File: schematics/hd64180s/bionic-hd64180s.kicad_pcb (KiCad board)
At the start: 2 copper layers, 25.4 x 68.6 mm, 13 parts, among them J1 Bionic-P135, J2 Bionic-P245, U1 HD64180SH, U2 11AA010-I/TT, U3 74AHCT157

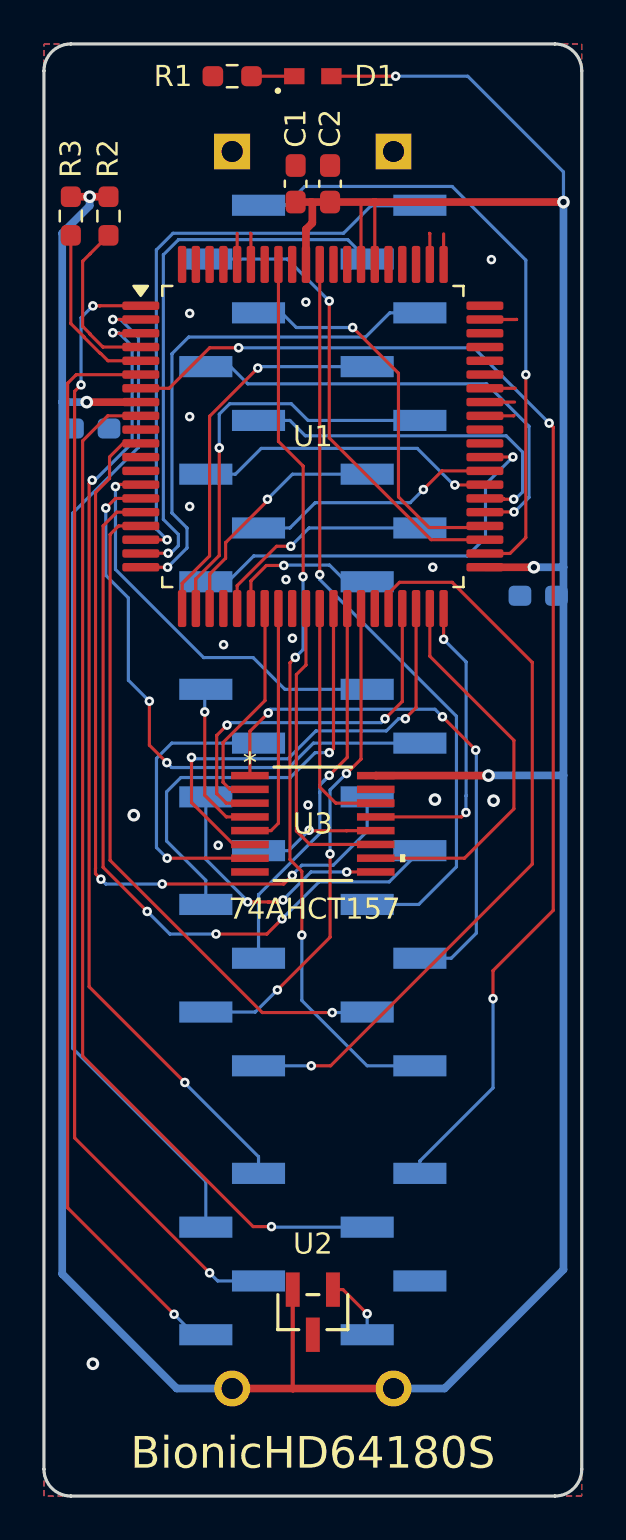
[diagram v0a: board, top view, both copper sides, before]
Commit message: [schematics] Straighten board tracks and regenerate Gerbers
straighten_tracks.py on every routed board: router leftovers snapped to
0/45/90 degrees and redundant segments merged, each pass DRC-checked
(counts unchanged). Gerbers and drill files of the changed boards are
regenerated with each board's plot settings, keeping the committed file
sets; tms9980 keeps its tracks (the rebuild left a dangling VCC stub).
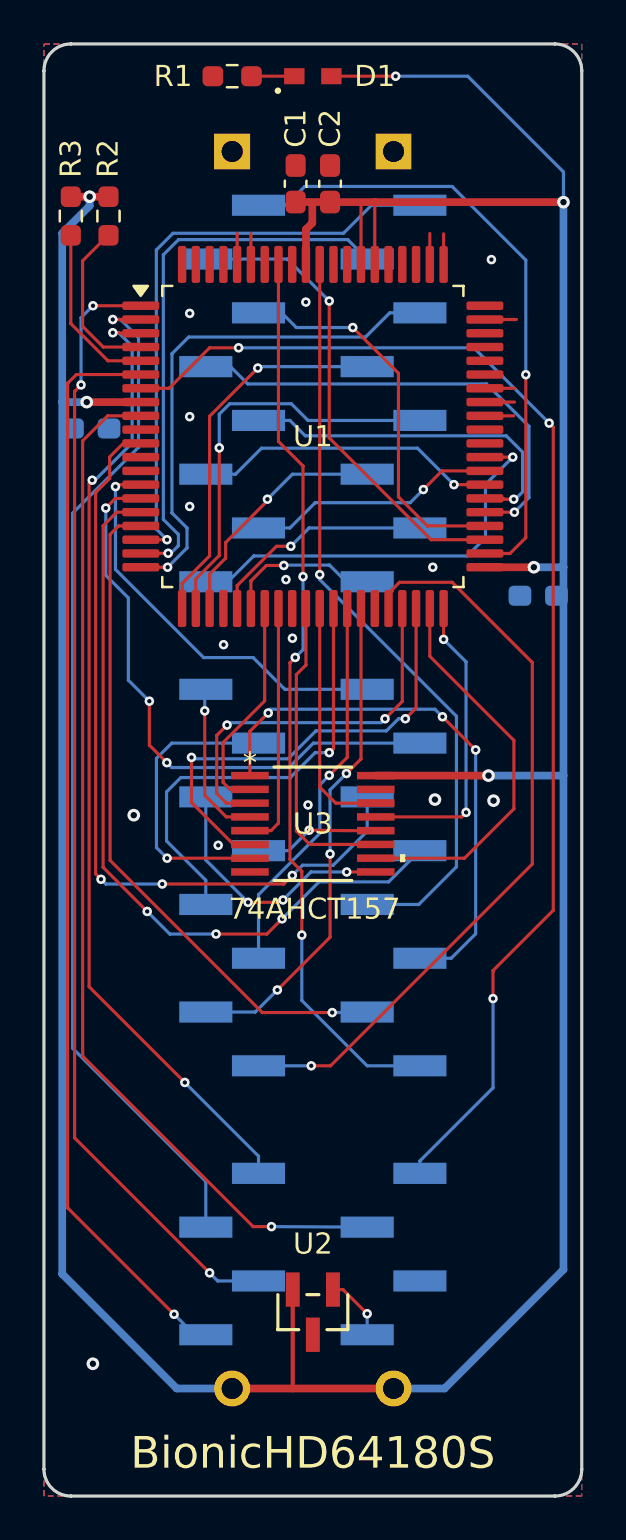
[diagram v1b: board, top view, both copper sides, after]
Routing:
- net D7: track 19.7 -> 17.9 mm
- net D2: track 18.3 -> 17.1 mm
- net D3: track 22.2 -> 21.0 mm
- net A7: track 7.43 -> 6.44 mm
- net D4: track 16.9 -> 16.0 mm
- net ~{LIR}: track 37.4 -> 36.6 mm
- net A17: track 22.0 -> 21.3 mm
- net A15: track 35.7 -> 35.0 mm
- net ~{INT0}: track 45.8 -> 45.1 mm
- net D5: track 14.4 -> 13.7 mm
- net ~{RESET}: track 51.6 -> 51.0 mm
- net A13: track 18.8 -> 18.3 mm

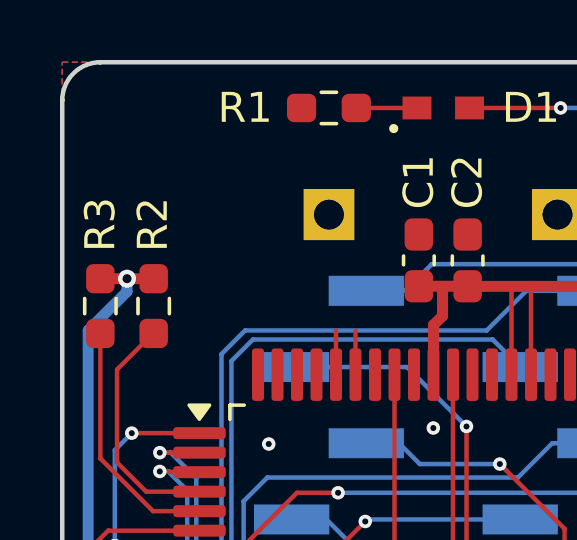
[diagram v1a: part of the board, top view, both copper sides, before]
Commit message: [schematics] Align silkscreen reference labels
align_silk.py snaps each footprint kind's labels onto their common
offset and angle and clears labels DRC flags on silkscreen; 76 labels on
22 boards, no DRC count grows. Their Gerbers are regenerated.
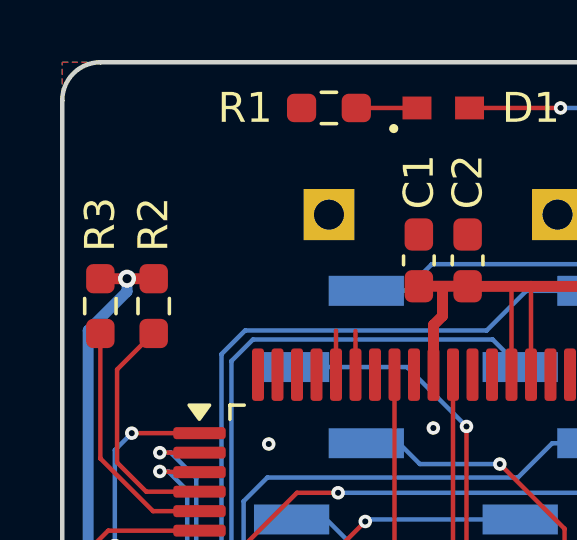
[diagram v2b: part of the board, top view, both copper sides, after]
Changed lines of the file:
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@@
 		(tags "resistor handsolder")
 		(property "Reference" "R3"
-			(at -2.7178 0 90)
+			(at -2.72 0.01 90)
 			(layer "F.SilkS")
 			(effects
@@
 		(tags "resistor handsolder")
 		(property "Reference" "R2"
-			(at -2.7178 0.0254 90)
+			(at -2.72 0.01 90)
 			(layer "F.SilkS")
 			(effects

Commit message: [schematics] Remove the JLC order-number marker from all boards
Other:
- board text removed: "JLCJLCJLCJLC"
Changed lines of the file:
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@@
-		)
-	)
-	(gr_text "JLCJLCJLCJLC"
-		(at 113.7 137.31 0)
-		(layer "B.SilkS")
-		(effects
-			(font
-				(size 0.8 0.8)
-			)
-			(justify bottom mirror)
 		)
 	)
